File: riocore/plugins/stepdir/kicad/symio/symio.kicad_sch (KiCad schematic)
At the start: 31 parts, among them J1 DE15_Pins_HighDensity, U1 MAX485E, U12 MAX485E, U17 ADuM1201BR, U2 MAX485E, U3 MAX485E, U4 MAX485E, U5 ADuM1201BR, U6 ADuM1201BR, U7 ADuM1201BR, U8 ADuM1201BR

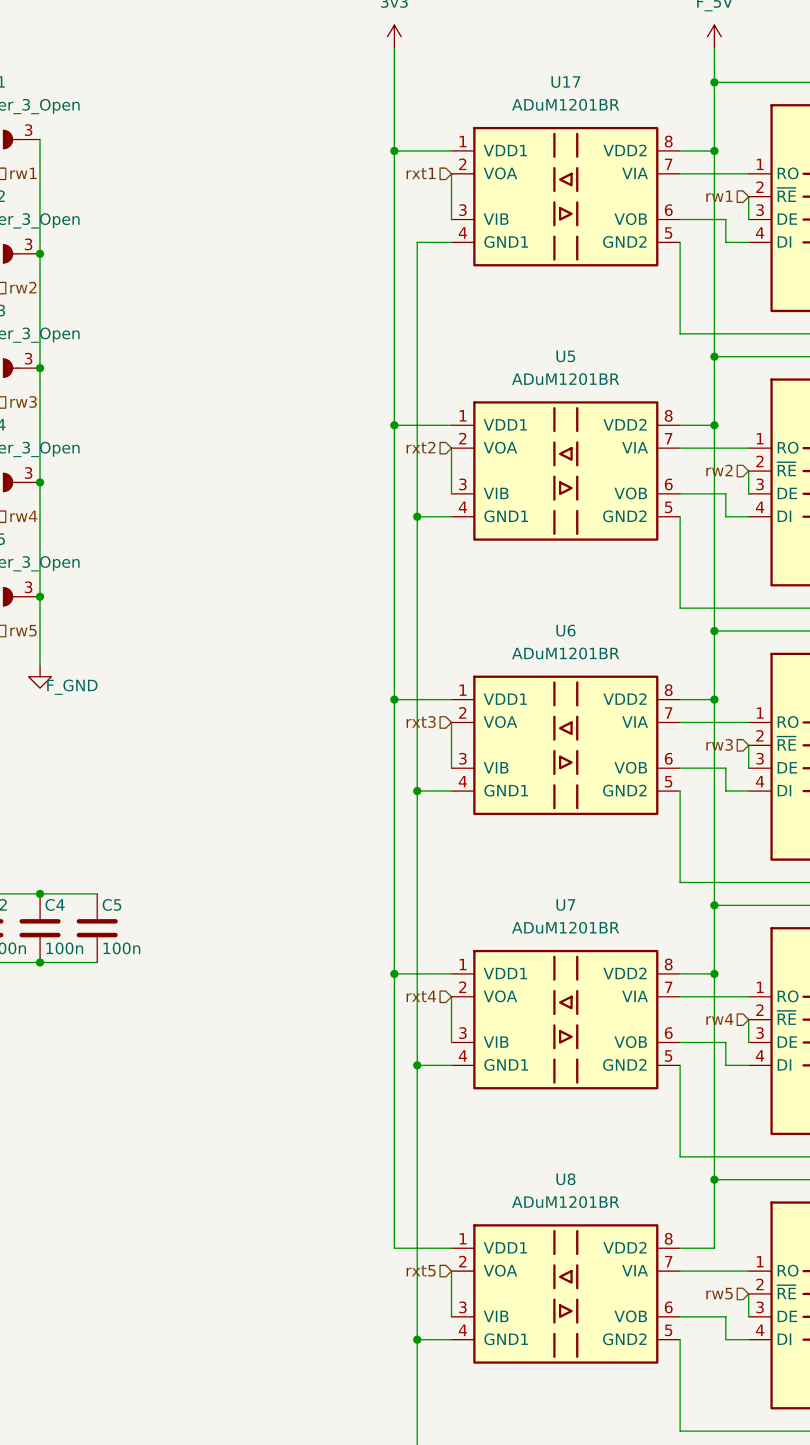
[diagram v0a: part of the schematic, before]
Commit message: kicad: pin positions
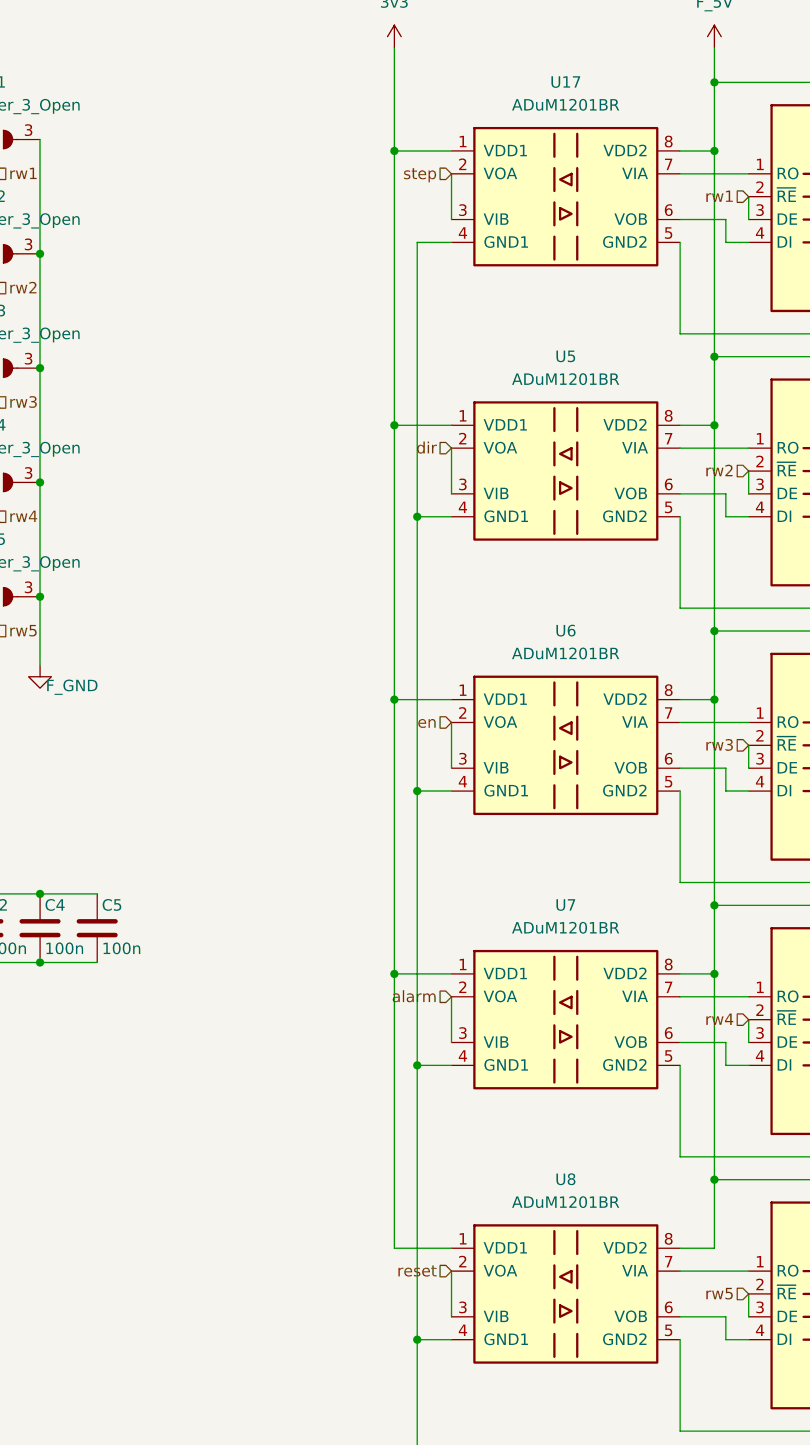
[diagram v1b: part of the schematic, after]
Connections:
- net rxt1 renamed step
- net rxt2 renamed dir
- net rxt3 renamed en
- net rxt4 renamed alarm
- net rxt5 renamed reset
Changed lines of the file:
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@@
 		)
 	)
-	(hierarchical_label "rxt2"
+	(hierarchical_label "dir"
 		(shape input)
 		(at 83.82 64.77 180)
@@
 		)
 	)
-	(hierarchical_label "rxt4"
+	(hierarchical_label "alarm"
 		(shape input)
 		(at 83.82 125.73 180)
@@
 		)
 	)
-	(hierarchical_label "rxt1"
+	(hierarchical_label "step"
 		(shape input)
 		(at 83.82 34.29 180)
@@
 		)
 	)
-	(hierarchical_label "rxt3"
+	(hierarchical_label "en"
 		(shape input)
 		(at 83.82 95.25 180)
@@
 		)
 	)
-	(hierarchical_label "rxt5"
+	(hierarchical_label "reset"
 		(shape input)
 		(at 83.82 156.21 180)
@@
 		)
 		(instances
-			(project ""
+			(project "symio"
 				(path "/51ba587e-33bb-4f51-926b-30833bf30ced"
 					(reference "J1")
@@
 		)
 		(instances
-			(project ""
+			(project "symio"
 				(path "/51ba587e-33bb-4f51-926b-30833bf30ced"
 					(reference "JP1")
